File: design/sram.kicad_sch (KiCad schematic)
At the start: 43 parts, among them U11 IS61WV12816EDBLL-10TLI

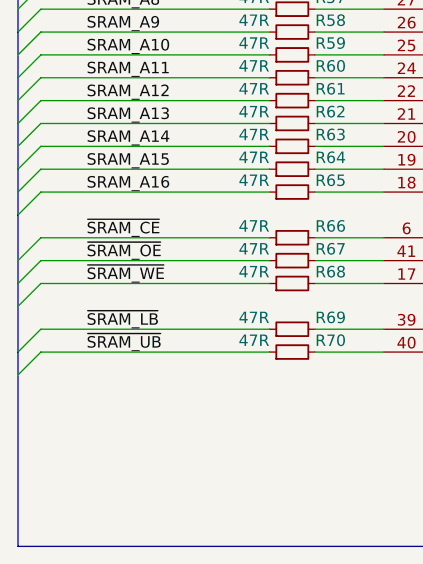
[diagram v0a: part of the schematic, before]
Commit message: Named button reset net
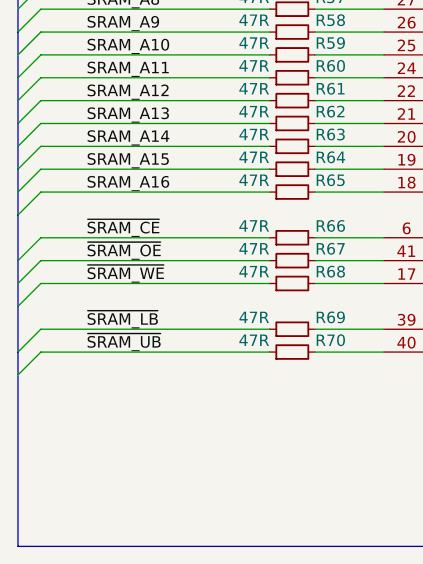
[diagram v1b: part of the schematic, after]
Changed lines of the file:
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@@
 (kicad_sch (version 20200512) (host eeschema "5.99.0-unknown-4efed4b~101~ubuntu18.04.1")
-  (page 6 8)
+  (page 1 8)
   (paper "A4")
   (title_block
@@
   (bus (pts (xy 36.83 96.52) (xy 36.83 101.6)))
   (bus (pts (xy 36.83 101.6) (xy 36.83 106.68)))
-  (bus (pts (xy 36.83 106.68) (xy 36.83 114.3)))
-  (bus (pts (xy 36.83 114.3) (xy 36.83 121.92)))
+  (bus (pts (xy 36.83 106.68) (xy 36.83 111.76)))
+  (bus (pts (xy 36.83 111.76) (xy 36.83 116.84)))
+  (bus (pts (xy 36.83 116.84) (xy 36.83 121.92)))
   (bus (pts (xy 36.83 121.92) (xy 36.83 143.51)))
   (bus (pts (xy 36.83 143.51) (xy 158.75 143.51)))

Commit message: Updated reset system
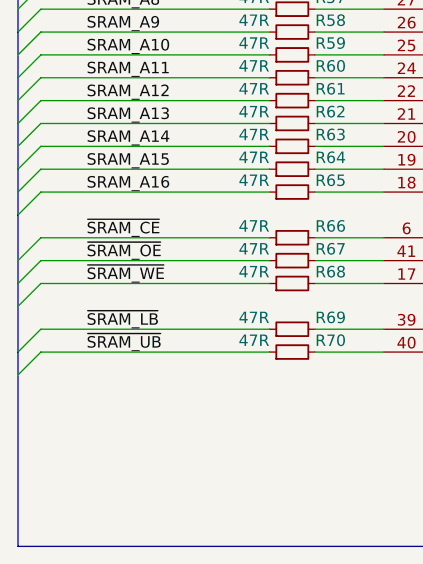
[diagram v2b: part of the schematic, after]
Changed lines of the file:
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@@
   (bus (pts (xy 36.83 96.52) (xy 36.83 101.6)))
   (bus (pts (xy 36.83 101.6) (xy 36.83 106.68)))
-  (bus (pts (xy 36.83 106.68) (xy 36.83 111.76)))
-  (bus (pts (xy 36.83 111.76) (xy 36.83 116.84)))
-  (bus (pts (xy 36.83 116.84) (xy 36.83 121.92)))
+  (bus (pts (xy 36.83 106.68) (xy 36.83 114.3)))
+  (bus (pts (xy 36.83 114.3) (xy 36.83 121.92)))
   (bus (pts (xy 36.83 121.92) (xy 36.83 143.51)))
   (bus (pts (xy 36.83 143.51) (xy 158.75 143.51)))

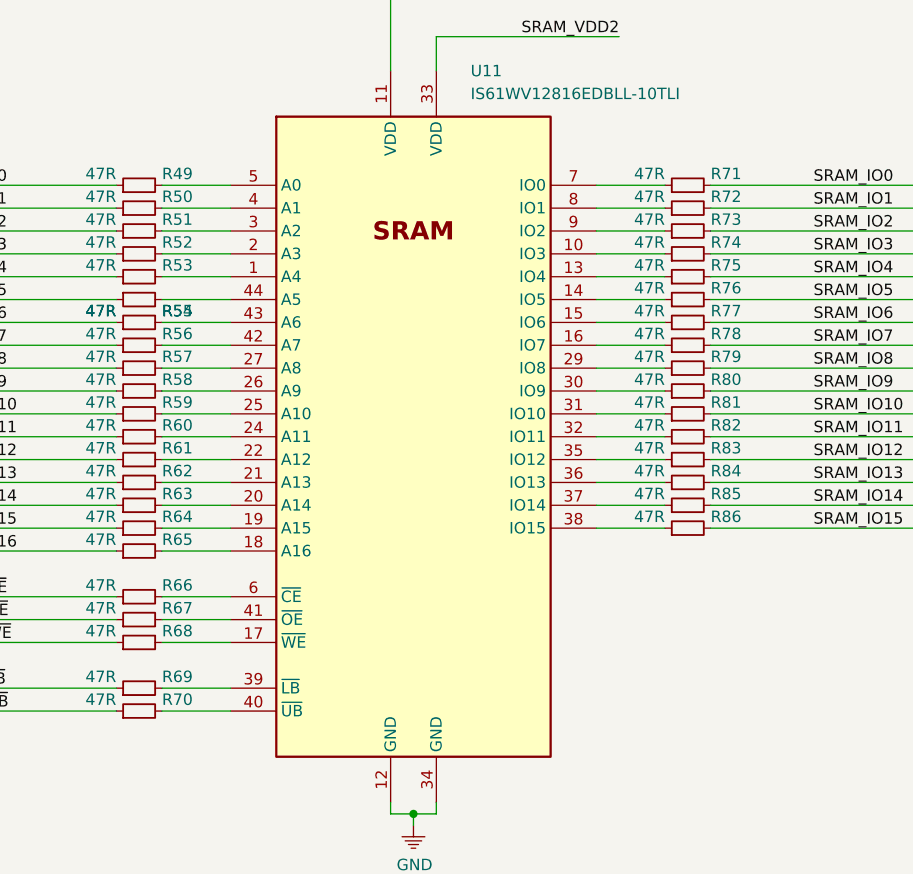
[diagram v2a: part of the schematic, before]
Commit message: Added fiducials
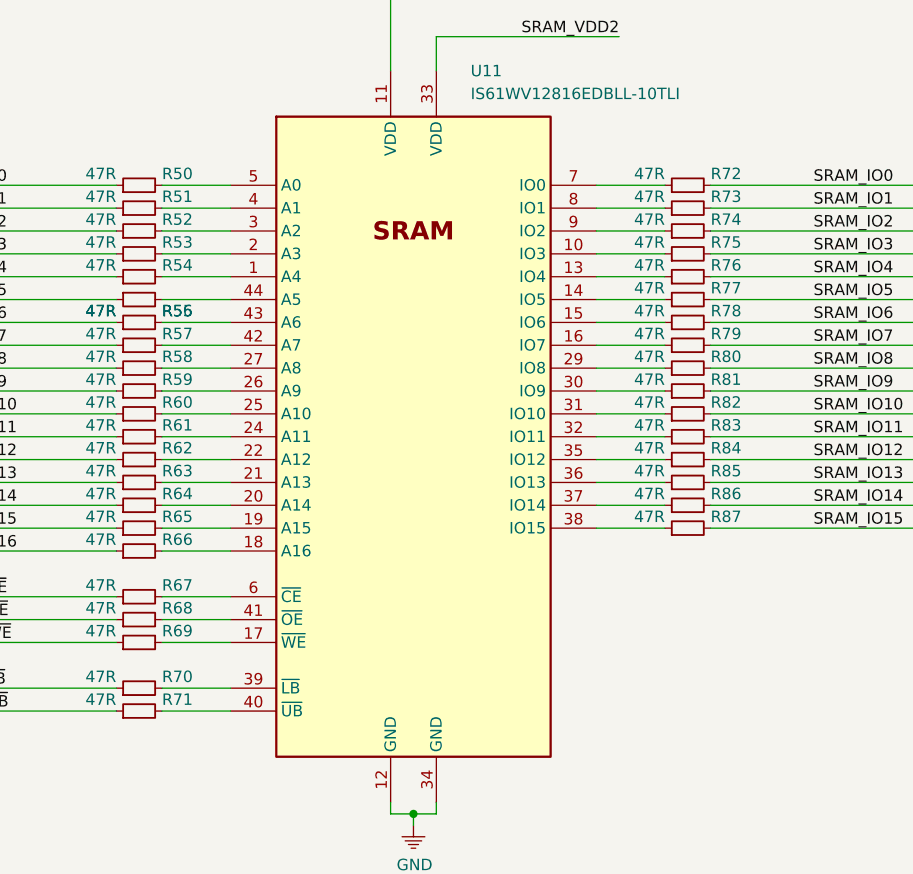
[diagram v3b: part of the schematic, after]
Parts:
- renumbered R49 to R50, R50 to R51, R51 to R52, R52 to R53, R53 to R54, R54 to R55, R55 to R56, R56 to R57, R57 to R58, R58 to R59, R59 to R60, R60 to R61, R61 to R62, R62 to R63, R63 to R64, R64 to R65, R65 to R66, R66 to R67, R67 to R68, R68 to R69, R69 to R70, R70 to R71, R71 to R72, R72 to R73, R73 to R74, R74 to R75, R75 to R76, R76 to R77, R77 to R78, R78 to R79, R79 to R80, R80 to R81, R81 to R82, R82 to R83, R83 to R84, R84 to R85, R85 to R86, R86 to R87

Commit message: Updated schematic
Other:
- note added: "VDD1 BYPASS"
- note added: "VDD2 BYPASS"
- moved on the sheet: C57, C58, C59, C60, R50, R51, R52, R53, R54, R55, R56, R57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
